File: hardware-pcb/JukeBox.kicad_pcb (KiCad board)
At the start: 2 copper layers, 90 x 90 mm, 74 parts, among them J1 USB4105-GF-A, J2 Conn_01x03, J3 Conn_01x04, J4 Conn_01x08, J5 Conn_01x01, J6 Conn_01x03, J7 Conn_01x03, J8 Conn_01x01, SW1 SW_SPST, SW10 SW_SPST, SW11 SW_SPST, SW12 SW_SPST, SW2 SW_SPST, SW3 SW_SPST, SW4 SW_SPST, SW5 SW_SPST, SW6 SW_SPST, SW7 SW_SPST, SW8 SW_SPST, SW9 SW_SPST, U1 NCP1117-3.3_SOT223, U2 W25Q128JVS, U3 RP2040, Y1 ECS-120-20-33-AEL-TR

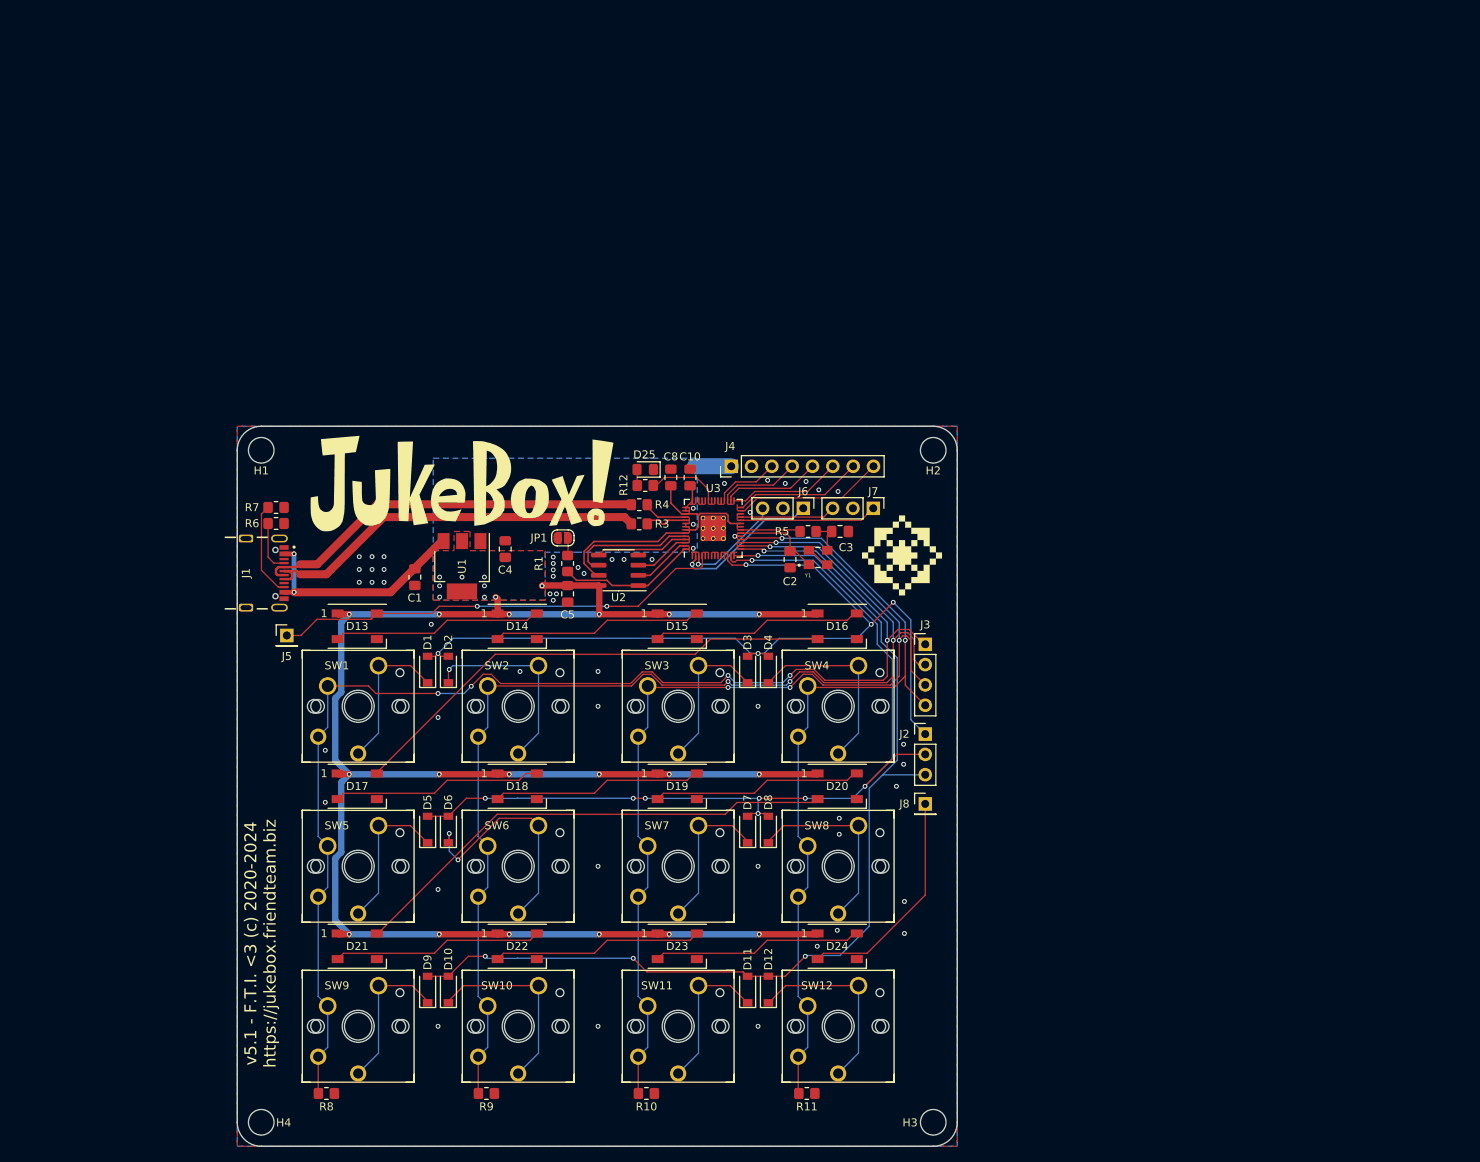
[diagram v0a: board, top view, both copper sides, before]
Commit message: change throughhole pins to test pads, start reassembling pcb
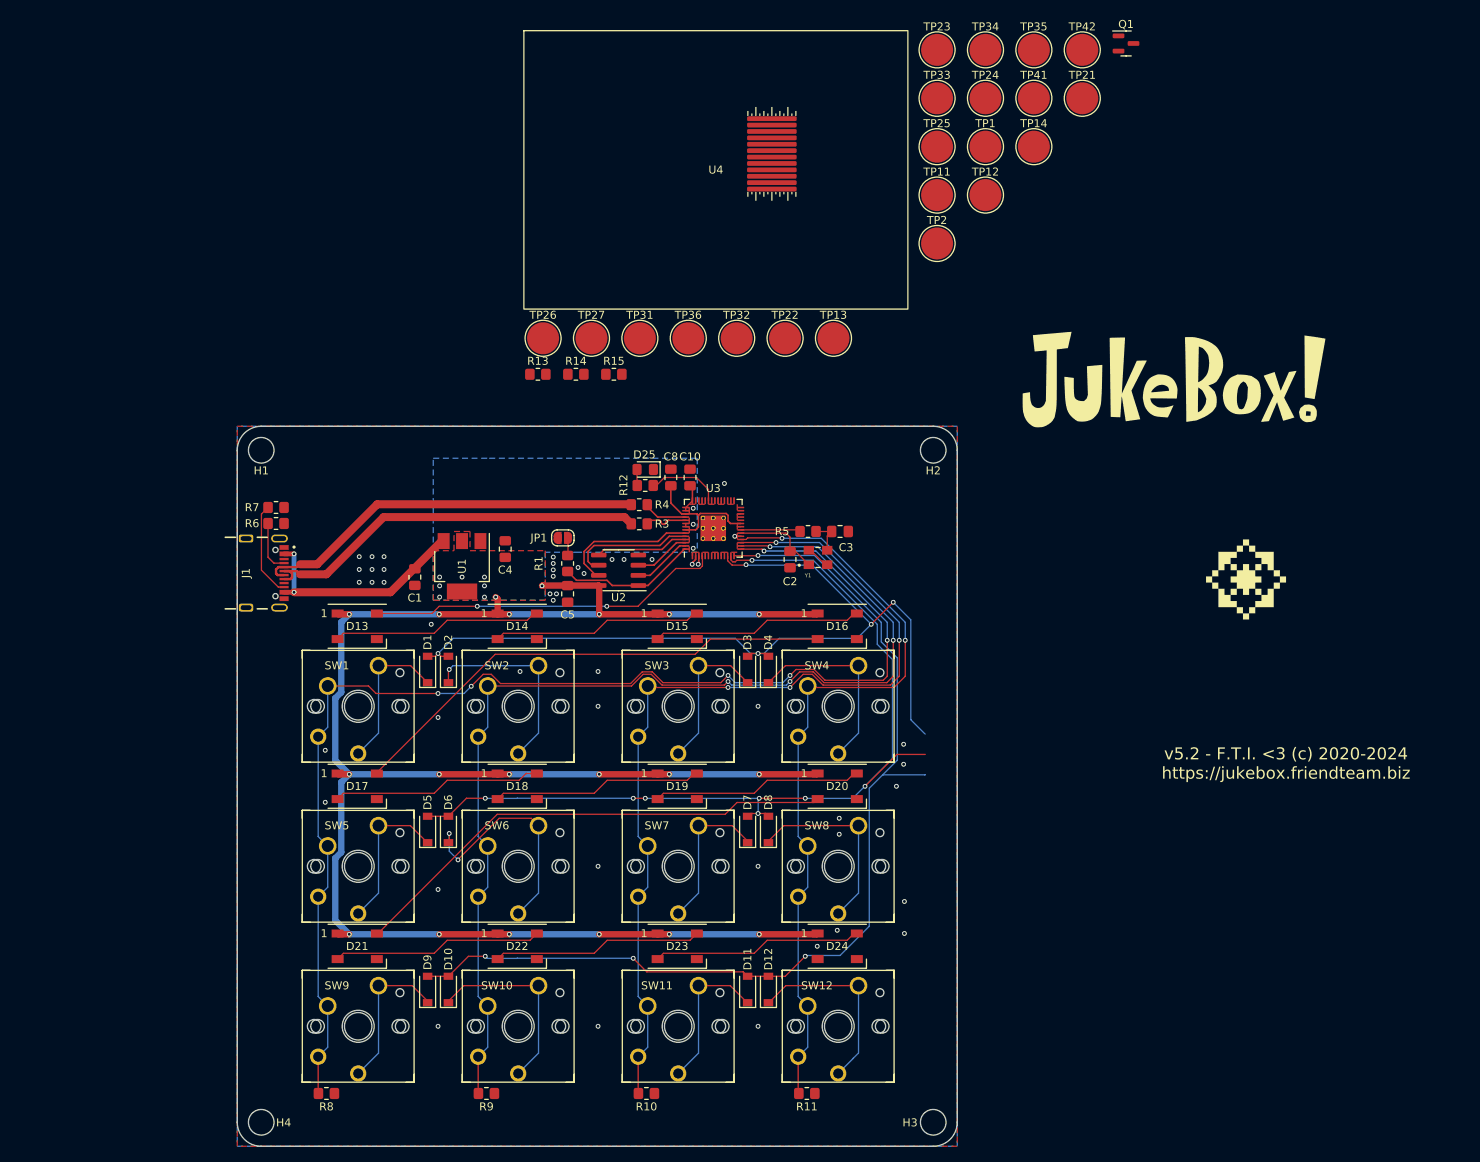
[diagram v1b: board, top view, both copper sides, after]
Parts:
- removed J2, J6, J7: Conn_01x03, Connector_PinHeader_2.54mm:PinHeader_1x03_P2.54mm_Vertical
- removed J3: Conn_01x04, Connector_PinHeader_2.54mm:PinHeader_1x04_P2.54mm_Vertical
- removed J4: Conn_01x08, Connector_PinHeader_2.54mm:PinHeader_1x08_P2.54mm_Vertical
- removed J5, J8: Conn_01x01, Connector_PinHeader_2.54mm:PinHeader_1x01_P2.54mm_Vertical
- added Q1: Q_NPN_ECB, Package_TO_SOT_SMD:SOT-23, F.Cu at (196.6, 59.0)
- added R13: 10, Resistor_SMD:R_0805_2012Metric_Pad1.20x1.40mm_HandSolder, F.Cu at (123.1, 100.3)
- added R14: 1k, Resistor_SMD:R_0805_2012Metric_Pad1.20x1.40mm_HandSolder, F.Cu at (127.8, 100.3)
- added R15: 10k, Resistor_SMD:R_0805_2012Metric_Pad1.20x1.40mm_HandSolder, F.Cu at (132.6, 100.3)
- added TP1: TestPoint, TestPoint:TestPoint_Pad_D4.0mm, F.Cu at (179.0, 71.9)
- added TP11: TestPoint, TestPoint:TestPoint_Pad_D4.0mm, F.Cu at (173.0, 78.0)
- added TP12: TestPoint, TestPoint:TestPoint_Pad_D4.0mm, F.Cu at (179.0, 78.0)
- added TP13: TestPoint, TestPoint:TestPoint_Pad_D4.0mm, F.Cu at (160.0, 95.8)
- added TP14: TestPoint, TestPoint:TestPoint_Pad_D4.0mm, F.Cu at (185.1, 71.9)
- added TP2: TestPoint, TestPoint:TestPoint_Pad_D4.0mm, F.Cu at (173.0, 84.0)
- added TP21: TestPoint, TestPoint:TestPoint_Pad_D4.0mm, F.Cu at (191.1, 65.8)
- added TP22: TestPoint, TestPoint:TestPoint_Pad_D4.0mm, F.Cu at (154.0, 95.8)
- added TP23: TestPoint, TestPoint:TestPoint_Pad_D4.0mm, F.Cu at (173.0, 59.8)
- added TP24: TestPoint, TestPoint:TestPoint_Pad_D4.0mm, F.Cu at (179.0, 65.8)
- added TP25: TestPoint, TestPoint:TestPoint_Pad_D4.0mm, F.Cu at (173.0, 71.9)
- added TP26: TestPoint, TestPoint:TestPoint_Pad_D4.0mm, F.Cu at (123.7, 95.8)
- added TP27: TestPoint, TestPoint:TestPoint_Pad_D4.0mm, F.Cu at (129.8, 95.8)
- added TP31: TestPoint, TestPoint:TestPoint_Pad_D4.0mm, F.Cu at (135.8, 95.8)
- added TP32: TestPoint, TestPoint:TestPoint_Pad_D4.0mm, F.Cu at (147.9, 95.8)
- added TP33: TestPoint, TestPoint:TestPoint_Pad_D4.0mm, F.Cu at (173.0, 65.8)
- added TP34: TestPoint, TestPoint:TestPoint_Pad_D4.0mm, F.Cu at (179.0, 59.8)
- added TP35: TestPoint, TestPoint:TestPoint_Pad_D4.0mm, F.Cu at (185.1, 59.8)
- added TP36: TestPoint, TestPoint:TestPoint_Pad_D4.0mm, F.Cu at (141.9, 95.8)
- added TP41: TestPoint, TestPoint:TestPoint_Pad_D4.0mm, F.Cu at (185.1, 65.8)
- added TP42: TestPoint, TestPoint:TestPoint_Pad_D4.0mm, F.Cu at (191.1, 59.8)
- added U4: st7789v, RP2040_minimal:st7789v, F.Cu at (145.3, 74.8)
- moved G1 89.9 mm to (202.6, 101.0)
- moved G*** 43.1 mm to (211.6, 126.0)
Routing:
- net /RGBDOUT: track 28.2 -> 0.00 mm
- net /GPIO16: track 18.9 -> 0.00 mm
- net /DBGRX: track 18.6 -> 1.25 mm
- net /DBGSC: track 17.2 -> 0.00 mm
- net /GPIO17: track 16.2 -> 0.00 mm
- net /GPIO18: track 14.1 -> 0.00 mm
- net /GPIO2: track 56.8 -> 44.4 mm
- net /GPIO19: track 12.3 -> 0.00 mm
- net /DBGSD: track 11.9 -> 0.00 mm
- net /DBGTX: track 12.7 -> 1.09 mm
- net /GPIO20: track 10.3 -> 0.00 mm
- net /GPIO14: track 125.6 -> 117.3 mm
- net /GPIO21: track 8.28 -> 0.00 mm
- net /GPIO13: track 144.6 -> 137.0 mm
- net /GPIO12: track 163.5 -> 157.4 mm
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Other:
- board text added: "v5.2 - F.T.I. <3 (c) 2020-2024 https://jukebox.friendteam.biz"
- board text removed: "v5.1 - F.T.I. <3 (c) 2020-2024 https://jukebox.friendteam.biz"

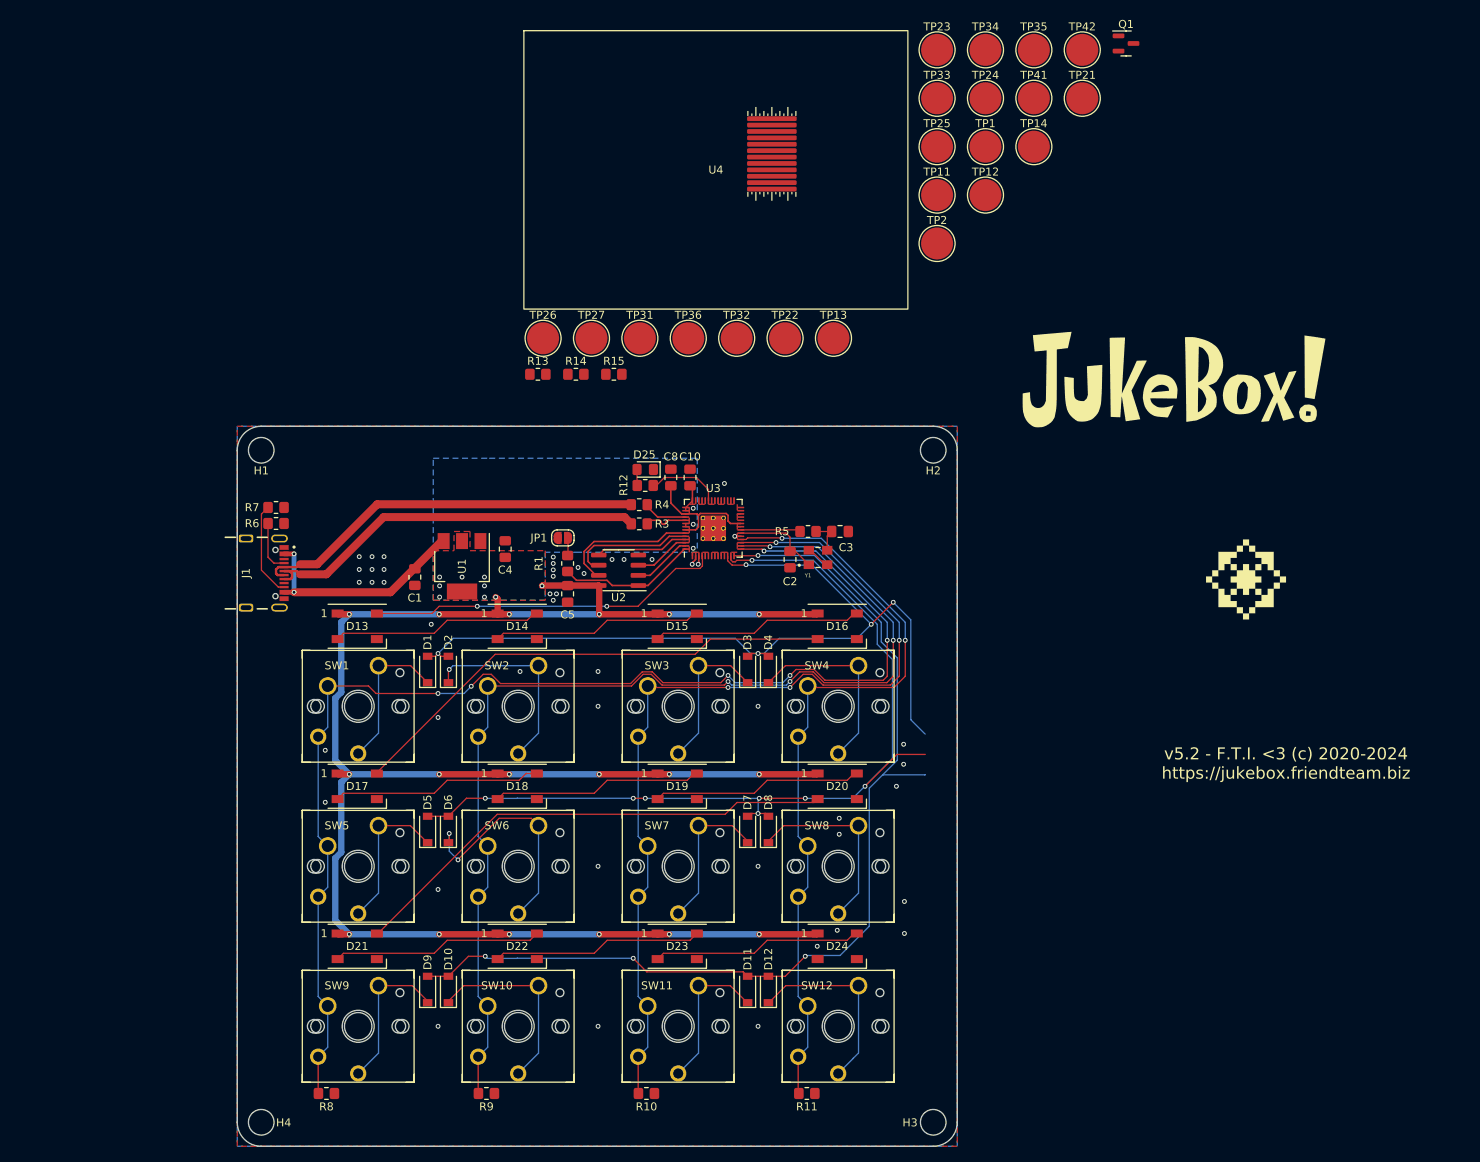
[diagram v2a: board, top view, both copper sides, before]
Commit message: rearrange board, new 100x100mm design
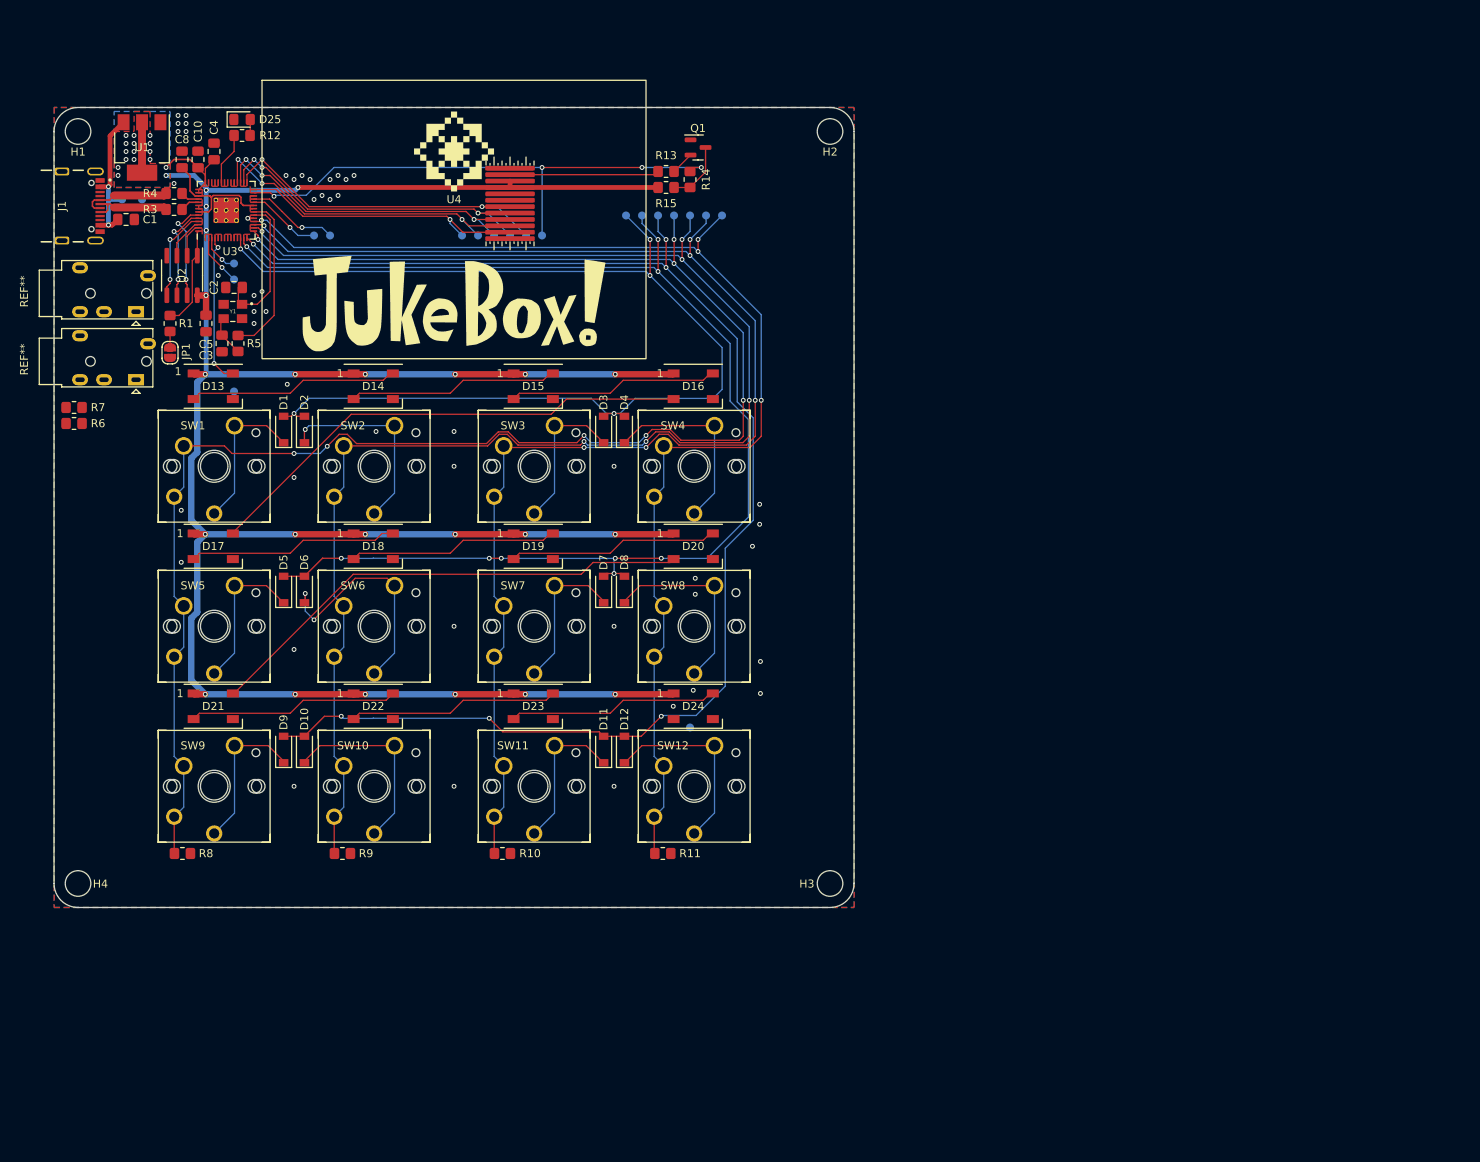
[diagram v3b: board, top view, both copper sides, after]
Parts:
- added G***: LOGO, RP2040_minimal:FTI, B.Cu at (112.6, 72.5)
- added G1: LOGO, RP2040_minimal:JukeBox, B.Cu at (112.6, 91.5)
- added REF**: Jack_3.5mm_PJ320E_Horizontal, Connector_Audio:Jack_3.5mm_PJ320E_Horizontal, F.Cu at (72.8, 101.0)
- added REF**: Jack_3.5mm_PJ320E_Horizontal, Connector_Audio:Jack_3.5mm_PJ320E_Horizontal, F.Cu at (72.8, 92.5)
- D1, D10, D11, D12, D2, D3, D4, D5, D6, D7, D8, D9: value DIODE -> type="D" model="DIODE" lib=""
- TP1, TP11, TP12, TP13, TP14, TP2, TP21, TP22, TP23, TP24, TP25, TP26, TP27, TP31, TP32, TP33, TP34, TP35, TP36, TP41, TP42: footprint TestPoint:TestPoint_Pad_D4.0mm -> TestPoint:TestPoint_Pad_D1.0mm; moved to B.Cu
- moved G*** 112.5 mm to (112.6, 72.5)
- moved TP1 108.1 mm to (71.1, 78.5), turned to 180 degrees
- moved TP41 106.5 mm to (85.1, 102.5), turned to 180 degrees
- moved TP2 99.5 mm to (73.6, 78.5), turned to 180 degrees
- moved TP42 97.9 mm to (142.1, 144.5), turned to 180 degrees
- moved TP12 94.5 mm to (85.1, 88.5), turned to 180 degrees
- moved TP14 90.7 mm to (95.1, 83.0)
- moved G1 90.5 mm to (112.6, 91.5)
- moved TP11 88.3 mm to (85.1, 86.5), turned to 180 degrees
- moved C3 80.7 mm to (83.6, 96.5), turned to 90 degrees
- moved Y1 79.4 mm to (84.9, 92.5), turned to 180 degrees
- moved C2 77.4 mm to (85.1, 89.5), turned to 180 degrees
- moved R5 75.0 mm to (85.6, 96.5), turned to -90 degrees
- moved C10 73.2 mm to (80.6, 73.5)
- moved C8 72.9 mm to (78.6, 73.5)
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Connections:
- U4 pad 3: +3.3V -> +3V3
- U4 pad 4: +3.3V -> +3V3
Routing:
- net +3V3: track 244.9 -> 336.0 mm, vias 30 -> 39
- net /GPIO16: track 0.00 -> 67.8 mm, vias 0 -> 4
- net /GPIO15: track 98.1 -> 155.6 mm, vias 2 -> 4
- net /GPIO14: track 117.3 -> 174.7 mm, vias 4 -> 6
- net /GPIO13: track 137.0 -> 194.1 mm, vias 4 -> 6
- net /GPIO12: track 157.4 -> 214.3 mm, vias 6 -> 8
- net /GPIO11: track 127.4 -> 179.0 mm, vias 4 -> 6
- net /GPIO10: track 115.1 -> 163.2 mm, vias 8 -> 9
- net /GPIO18: track 0.00 -> 44.1 mm, vias 0 -> 2
- net /GPIO19: track 0.00 -> 43.4 mm, vias 0 -> 3
- net /GPIO21: track 0.00 -> 43.2 mm, vias 0 -> 3
- net /GPIO20: track 0.00 -> 42.6 mm, vias 0 -> 3
- net /USB_D+: track 49.6 -> 11.2 mm
- net /USB_D-: track 49.4 -> 11.2 mm
- net /GPIO17: track 0.00 -> 36.9 mm, vias 0 -> 1
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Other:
- board size 90 x 90 mm -> 100 x 100 mm
